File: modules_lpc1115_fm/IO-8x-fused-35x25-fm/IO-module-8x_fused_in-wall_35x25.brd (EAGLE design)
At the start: 35 x 25 mm, 74 parts, among them IC1 LPC1115, IC2 ATAES132A-SHEQ-T, Q2 ASFL, U1 EEPROM, X3 MICROMATCH-10

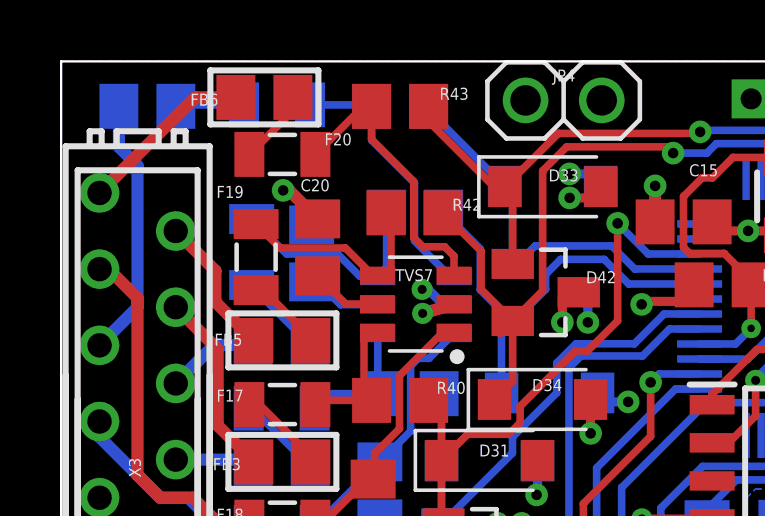
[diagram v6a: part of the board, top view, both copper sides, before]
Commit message: [IOmodule8xUP] vias added, Z-Diode Value changed
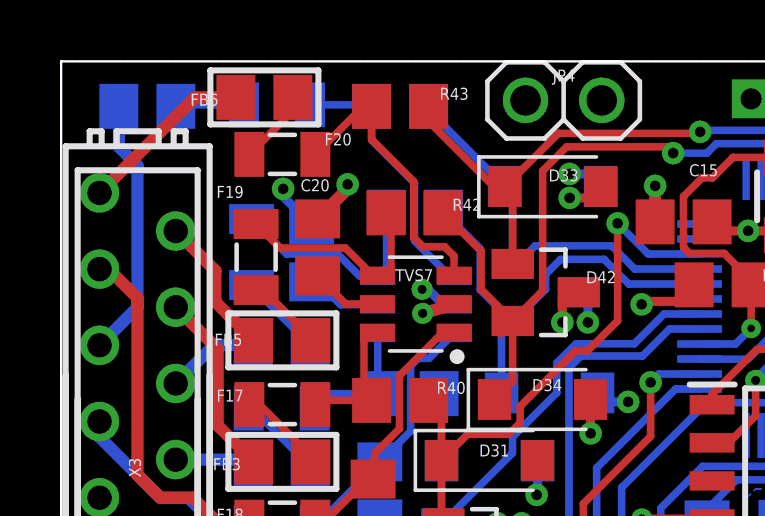
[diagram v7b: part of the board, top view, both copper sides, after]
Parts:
- D31: value DIODE -> DDZ9684
- D34: value DIODE -> PDZ3.3BGWJ
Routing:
- net GND: track 43.0 -> 44.6 mm, vias 23 -> 24
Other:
- board text removed: "N.A."
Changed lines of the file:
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@@
 <?xml version="1.0" encoding="utf-8"?>
 <!DOCTYPE eagle SYSTEM "eagle.dtd">
-<eagle version="9.6.1">
+<eagle version="9.6.2">
 <drawing>
 <settings>
@@
 <grid distance="0.05" unitdist="mm" unit="mm" style="dots" multiple="1" display="yes" altdistance="5" altunitdist="mil" altunit="mil"/>
 <layers>
-<layer number="1" name="Top" color="4" fill="1" visible="no" active="yes"/>
+<layer number="1" name="Top" color="4" fill="1" visible="yes" active="yes"/>
 <layer number="2" name="GND" color="1" fill="1" visible="no" active="yes"/>
 <layer number="3" name="Route3" color="4" fill="3" visible="no" active="no"/>
@@
 <layer number="14" name="Route14" color="1" fill="6" visible="no" active="no"/>
 <layer number="15" name="VCC" color="39" fill="1" visible="no" active="yes"/>
-<layer number="16" name="Bottom" color="1" fill="1" visible="no" active="yes"/>
+<layer number="16" name="Bottom" color="1" fill="1" visible="yes" active="yes"/>
 <layer number="17" name="Pads" color="2" fill="1" visible="yes" active="yes"/>
 <layer number="18" name="Vias" color="2" fill="1" visible="yes" active="yes"/>
@@
 <layer number="23" name="tOrigins" color="15" fill="1" visible="yes" active="yes"/>
 <layer number="24" name="bOrigins" color="15" fill="1" visible="yes" active="yes"/>
-<layer number="25" name="tNames" color="7" fill="1" visible="no" active="yes"/>
-<layer number="26" name="bNames" color="7" fill="1" visible="no" active="yes"/>
-<layer number="27" name="tValues" color="7" fill="1" visible="no" active="yes"/>
-<layer number="28" name="bValues" color="7" fill="1" visible="yes" active="yes"/>
+<layer number="25" name="tNames" color="7" fill="1" visible="yes" active="yes"/>
+<layer number="26" name="bNames" color="7" fill="1" visible="yes" active="yes"/>
+<layer number="27" name="tValues" color="7" fill="1" visible="yes" active="yes"/>
+<layer number="28" name="bValues" color="7" fill="1" visible="no" active="yes"/>
 <layer number="29" name="tStop" color="7" fill="3" visible="no" active="yes"/>
 <layer number="30" name="bStop" color="7" fill="6" visible="no" active="yes"/>
@@
 <text x="15.35" y="2.55" size="0.4" layer="51" ratio="6" rot="R40">BUS-V</text>
 <text x="12.7" y="2.55" size="0.4" layer="51" ratio="6" rot="R40">EIB OUT</text>
-<text x="22.75" y="23.15" size="0.4" layer="52" ratio="6" rot="MR220">GND</text>
-<text x="24.25" y="23.15" size="0.4" layer="52" ratio="6" rot="MR220">+3V3</text>
-<text x="25.75" y="23.15" size="0.4" layer="52" ratio="6" rot="MR220">SDA</text>
-<text x="27.3" y="23.15" size="0.4" layer="52" ratio="6" rot="MR220">SCL</text>
-<text x="28.8" y="23.15" size="0.4" layer="52" ratio="6" rot="MR220">N.A.</text>
-<circle x="21.7" y="23.25" radius="0.15" width="0.3048" layer="52"/>
+<text x="22.65" y="22.8" size="0.4" layer="51" ratio="6" rot="R320">GND</text>
+<text x="24.75" y="22.85" size="0.4" layer="51" ratio="6" rot="R320">+3V3</text>
+<text x="26.75" y="22.75" size="0.4" layer="51" ratio="6" rot="R320">SDA</text>
+<text x="28.7" y="22.7" size="0.4" layer="51" ratio="6" rot="R320">SCL</text>
 <circle x="32.8" y="5.5" radius="0.15" width="0.3048" layer="52"/>
 <circle x="1.3" y="6" radius="0.7" width="0.127" layer="52"/>
@@
 <attribute name="VALUE" x="7.98" y="20.01" size="0.4" layer="27"/>
 </element>
-<element name="D34" library="Diode" package="SODFL3718X115" package3d_urn="urn:adsk.eagle:package:9427153/2" value="DIODE" x="16.045" y="13.73" smashed="yes">
+<element name="D34" library="Diode" package="SODFL3718X115" package3d_urn="urn:adsk.eagle:package:9427153/2" value="PDZ3.3BGWJ" x="16.045" y="13.73" smashed="yes">
 <attribute name="CATEGORY" value="Diode" x="36.365" y="-7.86" size="1.778" layer="27" display="off"/>
 <attribute name="DESCRIPTION" value="" x="36.365" y="-7.86" size="1.778" layer="27" display="off"/>
@@
 <attribute name="VALUE" value="DIODE" x="15.695" y="13.3004" size="0.4" layer="27"/>
 </element>
-<element name="D31" library="Diode" package="SODFL3718X115" package3d_urn="urn:adsk.eagle:package:9427153/2" value="DIODE" x="14.28" y="11.7" smashed="yes">
+<element name="D31" library="Diode" package="SODFL3718X115" package3d_urn="urn:adsk.eagle:package:9427153/2" value="DDZ9684" x="14.28" y="11.7" smashed="yes">
 <attribute name="CATEGORY" value="Diode" x="48.57" y="7.89" size="1.778" layer="27" display="off"/>
 <attribute name="DESCRIPTION" value="" x="48.57" y="7.89" size="1.778" layer="27" display="off"/>
@@
 <attribute name="THERMALLOSS" value="" x="-6.9" y="-15.61" size="1.778" layer="28" rot="MR0" display="off"/>
 <attribute name="TYPE" value="" x="-6.9" y="-15.61" size="1.778" layer="28" rot="MR0" display="off"/>
-<attribute name="VALUE" value="DIODE" x="12.82" y="5.7504" size="0.4" layer="28" rot="MR0" align="top-center"/>
+<attribute name="VALUE" value="DIODE" x="12.97" y="5.7504" size="0.4" layer="28" rot="MR0" align="top-center"/>
 </element>
 <element name="D35" library="Diode" package="SODFL3718X115" package3d_urn="urn:adsk.eagle:package:9427153/2" value="DIODE" x="16.28" y="13.95" smashed="yes" rot="MR180">
@@
 <attribute name="MANUFACTURER" value="" x="50.57" y="17.76" size="1.778" layer="28" rot="MR180" display="off"/>
 <attribute name="MPN" value="" x="50.57" y="17.76" size="1.778" layer="28" rot="MR180" display="off"/>
-<attribute name="NAME" x="16.43" y="14.2704" size="0.4" layer="26" rot="MR180" align="bottom-center"/>
+<attribute name="NAME" x="16.68" y="14.4704" size="0.4" layer="26" rot="MR180" align="bottom-center"/>
 <attribute name="OPERATING_TEMP" value="" x="50.57" y="17.76" size="1.778" layer="28" rot="MR180" display="off"/>
 <attribute name="PART_STATUS" value="" x="50.57" y="17.76" size="1.778" layer="28" rot="MR180" display="off"/>
@@
 <attribute name="THERMALLOSS" value="" x="50.57" y="17.76" size="1.778" layer="28" rot="MR180" display="off"/>
 <attribute name="TYPE" value="" x="50.57" y="17.76" size="1.778" layer="28" rot="MR180" display="off"/>
-<attribute name="VALUE" value="DIODE" x="16.43" y="13.1296" size="0.4" layer="28" rot="MR180" align="top-center"/>
+<attribute name="VALUE" value="DIODE" x="16.68" y="13.5296" size="0.4" layer="28" rot="MR180" align="top-center"/>
 </element>
 <element name="D36" library="Diode" package="SODFL3718X115" package3d_urn="urn:adsk.eagle:package:9427153/2" value="DIODE" x="16.38" y="20.84" smashed="yes" rot="MR180">
@@
 <attribute name="MANUFACTURER" value="" x="36.7" y="34.81" size="1.778" layer="28" rot="MR180" display="off"/>
 <attribute name="MPN" value="" x="36.7" y="34.81" size="1.778" layer="28" rot="MR180" display="off"/>
-<attribute name="NAME" x="16.42" y="20.2396" size="0.4" layer="26" rot="MR0" align="bottom-center"/>
+<attribute name="NAME" x="16.77" y="20.9396" size="0.4" layer="26" rot="MR0" align="bottom-center"/>
 <attribute name="OPERATING_TEMP" value="" x="36.7" y="34.81" size="1.778" layer="28" rot="MR180" display="off"/>
 <attribute name="PART_STATUS" value="" x="36.7" y="34.81" size="1.778" layer="28" rot="MR180" display="off"/>
@@
 <attribute name="THERMALLOSS" value="" x="36.7" y="34.81" size="1.778" layer="28" rot="MR180" display="off"/>
 <attribute name="TYPE" value="" x="36.7" y="34.81" size="1.778" layer="28" rot="MR180" display="off"/>
-<attribute name="VALUE" value="DIODE" x="16.43" y="19.6196" size="0.4" layer="28" rot="MR180" align="top-center"/>
+<attribute name="VALUE" value="DIODE" x="16.78" y="20.3196" size="0.4" layer="28" rot="MR180" align="top-center"/>
 </element>
 <element name="D37" library="Diode" package="SODFL3718X115" package3d_urn="urn:adsk.eagle:package:9427153/2" value="DIODE" x="14.28" y="11.68" smashed="yes" rot="MR180">
@@
 </element>
 <element name="JP1" library="con-JST PH" package="B4B-PH-K-S" value="B4B-PH-K-S" x="26" y="23.75" smashed="yes" rot="MR0">
-<attribute name="NAME" x="27.15" y="21.72" size="0.4" layer="26" rot="MR0"/>
+<attribute name="NAME" x="26.95" y="20.92" size="0.4" layer="26" rot="MR0"/>
 <attribute name="VALUE" x="27.7" y="21.985" size="0.4" layer="28" rot="MR0" display="off"/>
 </element>
@@
 <wire x1="13.0854" y1="16.9" x2="12.05" y2="16.6" width="0.4064" layer="1"/>
 <via x="12.05" y="16.6" extent="1-16" drill="0.3"/>
-<wire x1="8.55" y1="19.75" x2="7.6" y2="20.7" width="0.4064" layer="1"/>
-<wire x1="7.6" y1="20.7" x2="7.4" y2="20.7" width="0.4064" layer="1"/>
-<via x="7.4" y="20.7" extent="1-16" drill="0.35"/>
+<wire x1="8.55" y1="19.75" x2="9.55" y2="20.75" width="0.4064" layer="1"/>
+<wire x1="9.55" y1="20.9" x2="9.55" y2="20.75" width="0.4064" layer="1"/>
+<via x="9.55" y="20.9" extent="1-16" drill="0.35"/>
 <via x="12.0325" y="17.4" extent="1-16" drill="0.3"/>
 <wire x1="12.7435" y1="16.89" x2="12.2335" y2="17.4" width="0.3048" layer="16"/>
@@
 <wire x1="12.3496" y1="5.55" x2="12.85" y2="5.55" width="0.3048" layer="16"/>
 <via x="12.85" y="5.55" extent="1-16" drill="0.35"/>
-<wire x1="15.8804" y1="11.68" x2="15.8804" y2="11.7" width="0" layer="19" extent="1-16"/>
-<wire x1="8.35" y1="19.55" x2="8.55" y2="19.75" width="0" layer="19" extent="1-16"/>
+<wire x1="7.4" y1="20.75" x2="7.4" y2="20.5" width="0.3048" layer="16"/>
+<wire x1="8.35" y1="19.55" x2="7.4" y2="20.5" width="0.3048" layer="16"/>
+<via x="7.4" y="20.75" extent="1-16" drill="0.35"/>
 </signal>
 <signal name="EIB_OUT">

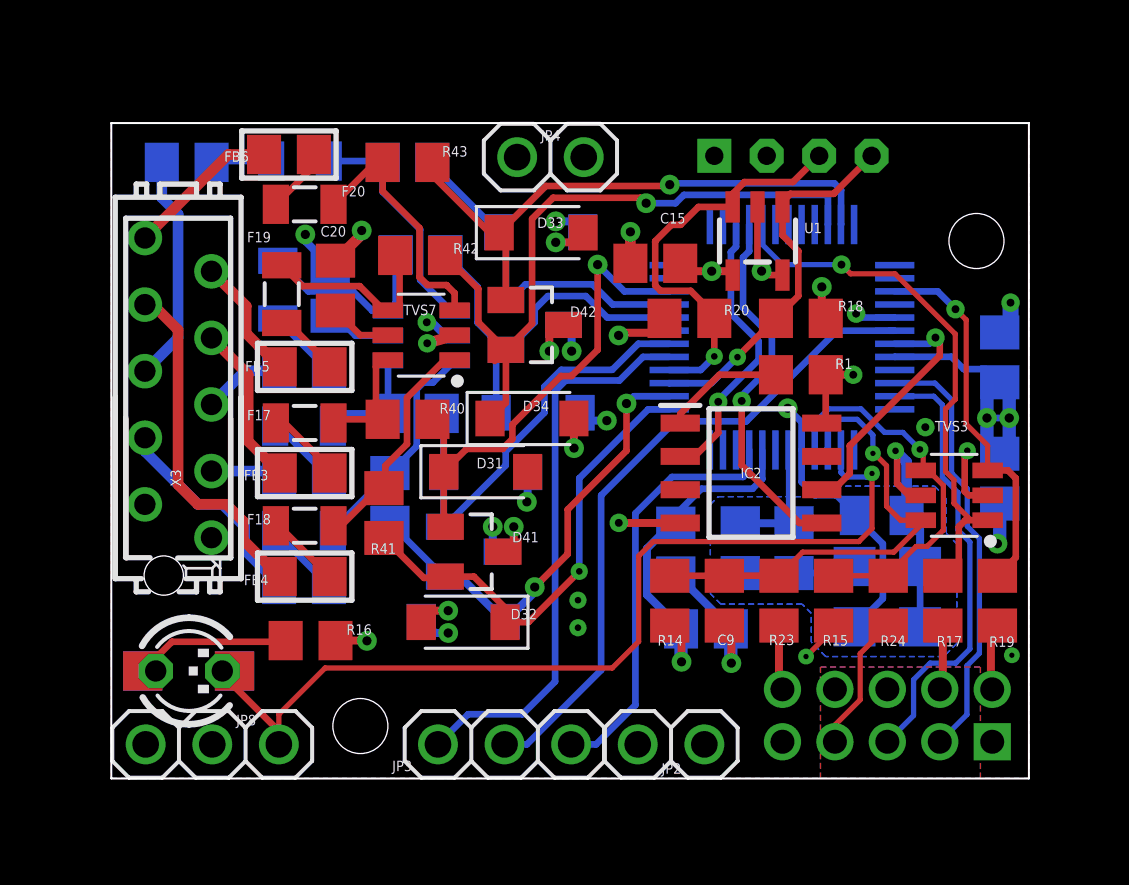
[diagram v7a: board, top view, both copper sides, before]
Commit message: [IOmodule8xUP] added 100R resistor to each IO
Protection of potential mess with 3V3 Z-Diodes when ARM pins run in high mode
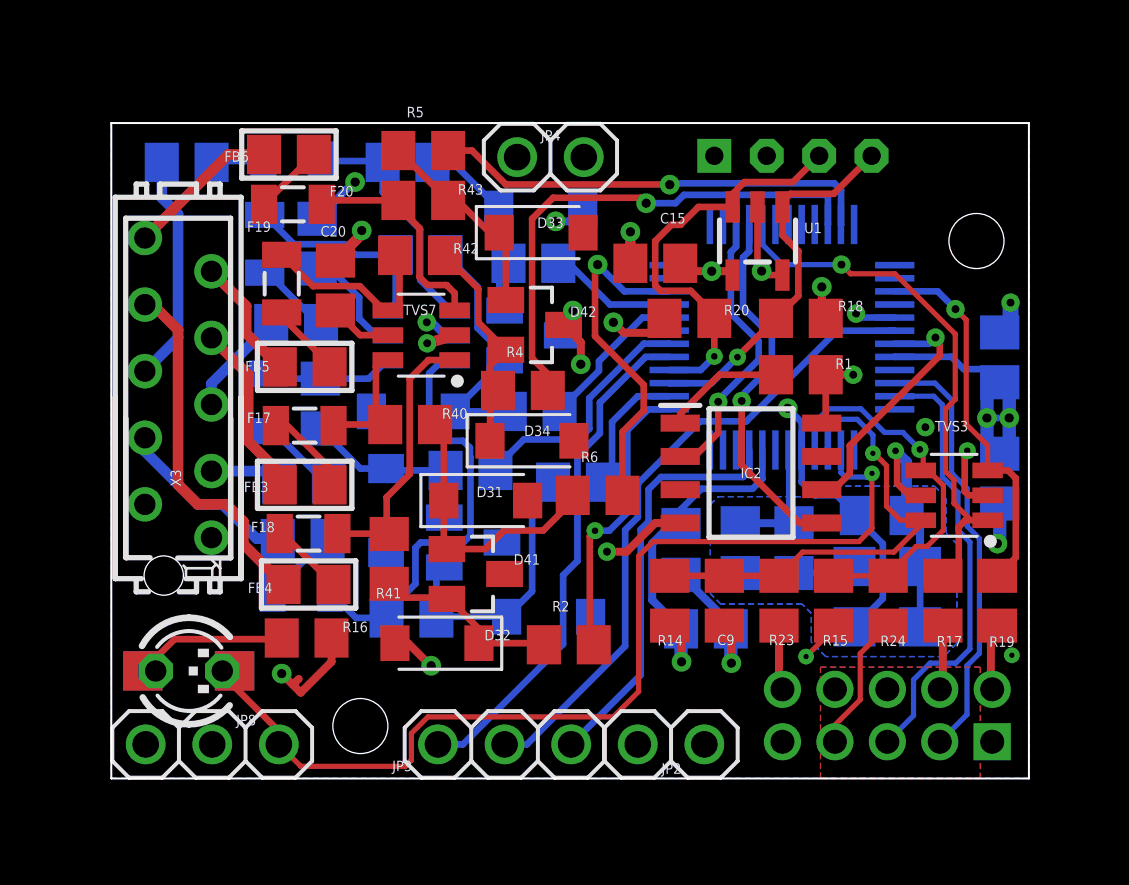
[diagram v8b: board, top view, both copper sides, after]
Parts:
- added R2, R3, R4, R5, R6, R7, R8, R9: 1k, rcl:R0805
- moved D35 4.76 mm to (11.5, 14.0), turned to 0 degrees
- moved R45 4.65 mm to (11.4, 6.12), turned to 180 degrees
- moved D37 4.07 mm to (10.5, 10.2), turned to 270 degrees
- moved R44 3.69 mm to (7.97, 14.3), turned to 270 degrees
- moved D38 3.27 mm to (16.7, 6.17), turned to 180 degrees
- moved F22 2.35 mm to (7.25, 7.11)
- moved C21 1.87 mm to (7.85, 20.4)
- moved FB8 1.82 mm to (7.05, 17.4)
- moved F23 1.82 mm to (5.85, 20.4)
- moved R41 1.76 mm to (10.6, 8.38)
- moved FB9 1.75 mm to (7.30, 9.15)
- moved F21 1.62 mm to (6.01, 14.3), turned to 90 degrees
- moved R43 1.57 mm to (11.9, 22.1)
- moved D32 1.28 mm to (12.4, 5.16)
- moved D31 1.10 mm to (14.3, 10.6)
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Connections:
- new net IO1B: D37.1, D40.2, R44.2, R9.1
- new net IO2B: D38.1, D40.1, R3.1, R45.2
- new net IO3B: D35.1, D39.1, R46.2, R7.1
- new net IO4B: D36.1, D39.2, R47.2, R8.1
- new net IO5B: D31.1, D41.1, R40.2, R6.1
- new net IO6B: D32.1, D41.2, R2.1, R41.2
- new net IO7B: D34.1, D42.2, R4.1, R42.2
- new net IO8B: D33.1, D42.1, R43.2, R5.1
- net IO1: now also R9.2; no longer D37.1, D40.2, R44.2
- net IO2: now also R3.2; no longer D38.1, D40.1, R45.2
- net IO3: now also R7.2; no longer D35.1, D39.1, R46.2
- net IO4: now also R8.2; no longer D36.1, D39.2, R47.2
- net IO5: now also R6.2; no longer D31.1, D41.1, R40.2
- net IO6: now also R2.2; no longer D32.1, D41.2, R41.2
- net IO7: now also R4.2; no longer D34.1, D42.2, R42.2
- net IO8: now also R5.2; no longer D33.1, D42.1, R43.2
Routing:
- net IO2: track 17.9 -> 5.03 mm, vias 2 -> 0
- net IO5B: track 0.00 -> 10.7 mm
- net IO2B: track 0.00 -> 10.6 mm
- net IO3B: track 0.00 -> 9.75 mm
- net IO7B: track 0.00 -> 9.14 mm
- net IO3: track 14.9 -> 5.91 mm
- net IO4: track 13.2 -> 4.88 mm
- net N$9: track 8.62 -> 16.8 mm
- net IO8B: track 0.00 -> 7.82 mm
- net IO1: track 17.1 -> 9.38 mm
- net IO1B: track 0.00 -> 7.26 mm
- net IO4B: track 0.00 -> 7.24 mm
- net IO6B: track 0.00 -> 7.19 mm
- net IO6: track 18.0 -> 11.1 mm
- net IO7: track 26.4 -> 19.7 mm
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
